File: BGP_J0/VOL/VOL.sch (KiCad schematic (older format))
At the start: 24 parts, among them P1 CONN_01X03, P2 CONN_01X02, P3 CONN_01X04, P4 CONN_01X03, Q1 J201, Q2 J201

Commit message: Schematics done, pcb layout pending
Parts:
- C2: value 10u -> 47u
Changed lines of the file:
@@
 	0    1    1    0
-$EndComp
-$Comp
-L CP1_Small C2
-U 1 1 5A6FC1F6
-P 3850 4600
-F 0 "C2" H 3860 4670 50  0000 L CNN
-F 1 "10u" H 3860 4520 50  0000 L CNN
-F 2 "Capacitors_Tantalum_SMD:TantalC_SizeR_EIA-2012" H 3850 4600 50  0001 C CNN
-F 3 "" H 3850 4600 50  0000 C CNN
-	1    3850 4600
-	1    0    0    -1
 $EndComp
 Wire Wire Line
@@
 	1    0    0    -1
 $EndComp
+$Comp
+L CP1_Small C2
+U 1 1 5A6FE715
+P 3850 4600
+F 0 "C2" H 3860 4670 50  0000 L CNN
+F 1 "47u" H 3860 4520 50  0000 L CNN
+F 2 "Capacitors_Tantalum_SMD:TantalC_SizeR_EIA-2012" H 3850 4600 50  0001 C CNN
+F 3 "" H 3850 4600 50  0000 C CNN
+	1    3850 4600
+	1    0    0    -1
+$EndComp

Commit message: PCB Layout done
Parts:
- removed P4: CONN_01X03, Connectors_JST:JST_PH_B3B-PH-K_03x2.00mm_Straight, symbol CONN_01X03
- added D1: D_Small, Diodes_SMD:SMA_Standard, symbol D_Small
- added P4: CONN_01X02, Connectors_JST:JST_PH_B2B-PH-K_02x2.00mm_Straight, symbol CONN_01X02
- Q1, Q2: value J201 -> J202; footprint TO_SOT_Packages_SMD:SOT-23 -> TO_SOT_Packages_SMD:SC-59
- R4: value 10k -> 12k
- R5: value 4.99k -> 6.8k
- R7: value 4.99k -> 10k
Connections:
- net Earth: now also C2.2, R3.2, D1.2 (A)
- net I_BY: now also P4.2 (P2)
- net O_BY: now also P4.1 (P1)
- net VCC: now also D1.1 (K)
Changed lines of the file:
@@
 P 4250 3350
 F 0 "Q1" H 4550 3400 50  0000 R CNN
-F 1 "J201" H 4600 3300 50  0000 R CNN
-F 2 "TO_SOT_Packages_SMD:SOT-23" H 4450 3450 50  0001 C CNN
+F 1 "J202" H 4600 3300 50  0000 R CNN
+F 2 "TO_SOT_Packages_SMD:SC-59" H 4450 3450 50  0001 C CNN
 F 3 "" H 4250 3350 50  0000 C CNN
 	1    4250 3350
@@
 P 4350 3000
 F 0 "R4" H 4380 3020 50  0000 L CNN
-F 1 "10k" H 4380 2960 50  0000 L CNN
+F 1 "12k" H 4380 2960 50  0000 L CNN
 F 2 "Resistors_SMD:R_0603_HandSoldering" H 4350 3000 50  0001 C CNN
 F 3 "" H 4350 3000 50  0000 C CNN
@@
 P 4350 3700
 F 0 "R5" H 4380 3720 50  0000 L CNN
-F 1 "4.99k" H 4380 3660 50  0000 L CNN
+F 1 "6.8k" H 4380 3660 50  0000 L CNN
 F 2 "Resistors_SMD:R_0603_HandSoldering" H 4350 3700 50  0001 C CNN
 F 3 "" H 4350 3700 50  0000 C CNN
@@
 P 5750 3150
 F 0 "Q2" H 6050 3200 50  0000 R CNN
-F 1 "J201" H 6100 3100 50  0000 R CNN
-F 2 "TO_SOT_Packages_SMD:SOT-23" H 5950 3250 50  0001 C CNN
+F 1 "J202" H 6100 3100 50  0000 R CNN
+F 2 "TO_SOT_Packages_SMD:SC-59" H 5950 3250 50  0001 C CNN
 F 3 "" H 5750 3150 50  0000 C CNN
 	1    5750 3150
@@
 P 5850 3550
 F 0 "R7" H 5880 3570 50  0000 L CNN
-F 1 "4.99k" H 5880 3510 50  0000 L CNN
+F 1 "10k" H 5880 3510 50  0000 L CNN
 F 2 "Resistors_SMD:R_0603_HandSoldering" H 5850 3550 50  0001 C CNN
 F 3 "" H 5850 3550 50  0000 C CNN
@@
 	3550 4700 3550 4750
 Wire Wire Line
-	3550 4750 3850 4750
+	3300 4750 3850 4750
 Wire Wire Line
 	3850 4750 3850 4700
@@
 $EndComp
 $Comp
-L CONN_01X03 P4
-U 1 1 5A6FC51C
-P 8400 4100
-F 0 "P4" H 8400 4300 50  0000 C CNN
-F 1 "CONN_01X03" V 8500 4100 50  0000 C CNN
-F 2 "Connectors_JST:JST_PH_B3B-PH-K_03x2.00mm_Straight" H 8400 4100 50  0001 C CNN
-F 3 "" H 8400 4100 50  0000 C CNN
-	1    8400 4100
-	1    0    0    -1
-$EndComp
-$Comp
-L Earth #PWR014
-U 1 1 5A6FC6BE
-P 8200 4200
-F 0 "#PWR014" H 8200 3950 50  0001 C CNN
-F 1 "Earth" H 8200 4050 50  0001 C CNN
-F 2 "" H 8200 4200 50  0000 C CNN
-F 3 "" H 8200 4200 50  0000 C CNN
-	1    8200 4200
-	1    0    0    -1
-$EndComp
-$Comp
 L CP1_Small C2
 U 1 1 5A6FE715
@@
 	1    0    0    -1
 $EndComp
+$Comp
+L CONN_01X02 P4
+U 1 1 5A712F0B
+P 8400 4050
+F 0 "P4" H 8400 4200 50  0000 C CNN
+F 1 "CONN_01X02" V 8500 4050 50  0000 C CNN
+F 2 "Connectors_JST:JST_PH_B2B-PH-K_02x2.00mm_Straight" H 8400 4050 50  0001 C CNN
+F 3 "" H 8400 4050 50  0000 C CNN
+	1    8400 4050
+	1    0    0    -1
+$EndComp
+$Comp
+L Earth #PWR014
+U 1 1 5A71310A
+P 3550 4750
+F 0 "#PWR014" H 3550 4500 50  0001 C CNN
+F 1 "Earth" H 3550 4600 50  0001 C CNN
+F 2 "" H 3550 4750 50  0000 C CNN
+F 3 "" H 3550 4750 50  0000 C CNN
+	1    3550 4750
+	1    0    0    -1
+$EndComp
+$Comp
+L D_Small D1
+U 1 1 5A71407F
+P 3300 4600
+F 0 "D1" H 3250 4680 50  0000 L CNN
+F 1 "D_Small" H 3150 4520 50  0000 L CNN
+F 2 "Diodes_SMD:SMA_Standard" V 3300 4600 50  0001 C CNN
+F 3 "" V 3300 4600 50  0000 C CNN
+	1    3300 4600
+	0    1    1    0
+$EndComp
+Wire Wire Line
+	3300 4500 3300 4150
+Wire Wire Line
+	3300 4150 3550 4150
+Wire Wire Line
+	3300 4700 3300 4750
+Connection ~ 3550 4750
 $EndSCHEMATC

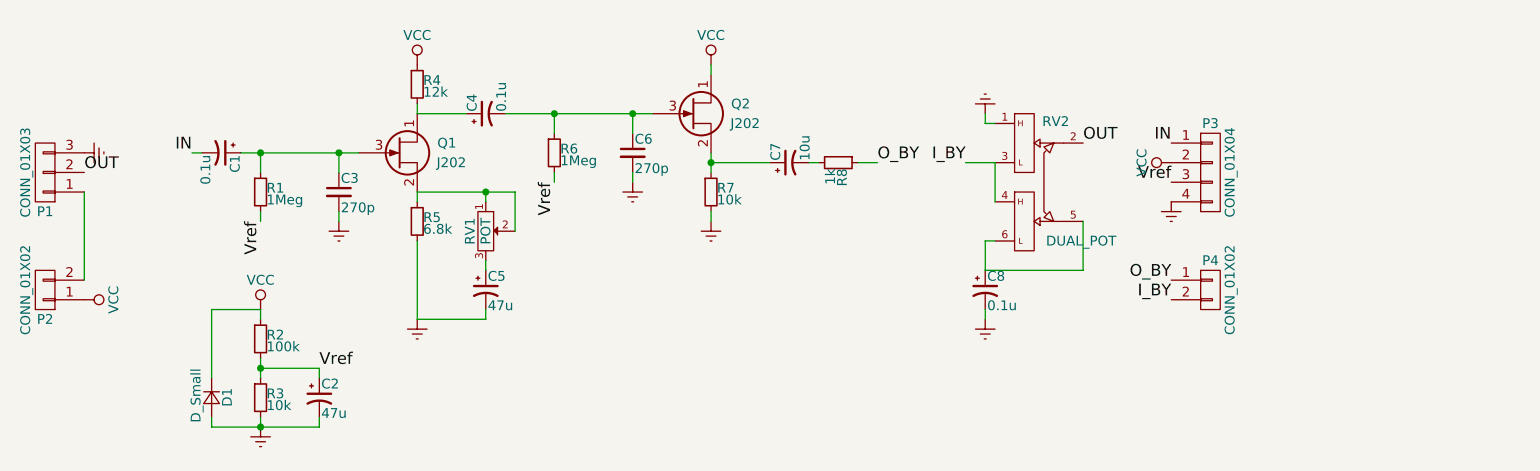
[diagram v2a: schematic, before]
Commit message: Changed POT, parallel VOL pot conn for offboard pot
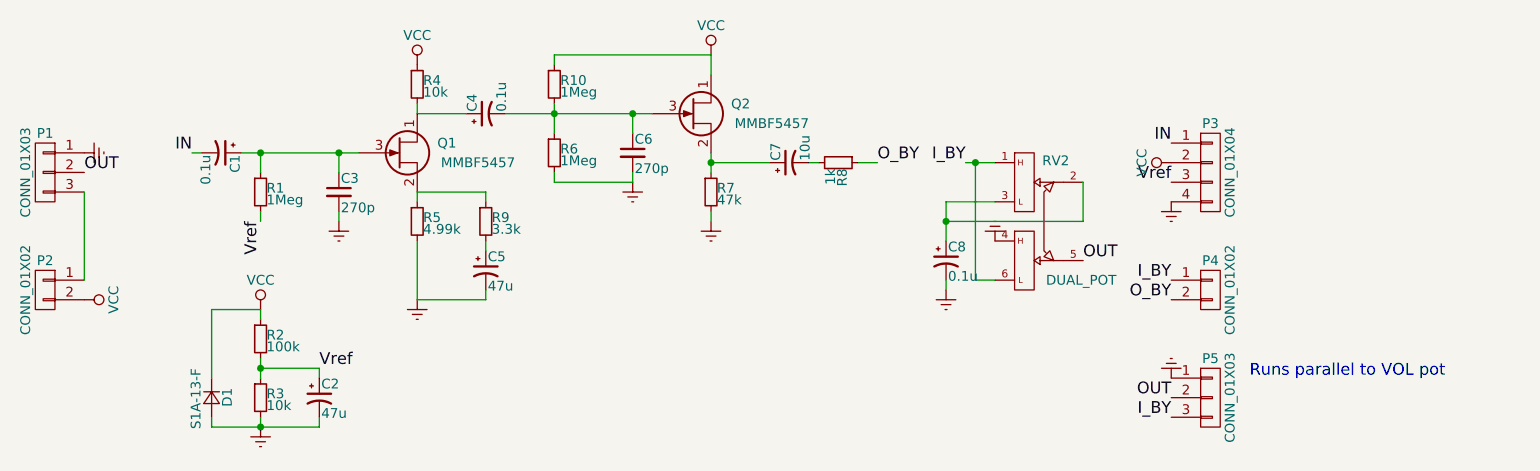
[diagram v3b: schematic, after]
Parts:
- removed RV1: POT, Potentiometers:Potentiometer_Trimmer_Bourns_3296W, symbol POT
- added P5: CONN_01X03, Connectors_JST:JST_PH_B3B-PH-K_03x2.00mm_Straight, symbol CONN_01X03
- added R10: 1Meg, Resistors_SMD:R_0603_HandSoldering, symbol R_Small
- added R9: 3.3k, Resistors_SMD:R_0603_HandSoldering, symbol R_Small
- D1: value D_Small -> S1A-13-F
- Q1, Q2: value J202 -> MMBF5457
- R4: value 12k -> 10k
- R5: value 6.8k -> 4.99k
- R7: value 10k -> 47k
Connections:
- net Earth: now also P1.1 (P1), R6.2, RV2.4, P5.1 (P1); no longer P1.3 (P3), RV2.1
- net I_BY: now also P4.1 (P1), RV2.1, RV2.6, P5.3 (P3); no longer P4.2 (P2), RV2.3, RV2.4
- net OUT: now also RV2.5, P5.2 (P2); no longer RV2.2
- net O_BY: now also P4.2 (P2); no longer P4.1 (P1)
- net VCC: now also P2.2 (P2), R10.1; no longer P2.1 (P1)
- net Vref: no longer R6.2
- net at Q1.2 (S), R5.1: now also R9.1
- net at C5.1: now also R9.2
- net at C4.2, C6.1, Q2.3 (G)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: now also R10.2
- new net: P1.3 (P3), P2.1 (P1)
- new net: C8.1, RV2.2, RV2.3
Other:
- note added: "Runs parallel to VOL pot"
- moved on the sheet: C5, C8, RV2
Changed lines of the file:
@@
 F 3 "" H 2450 3450 50  0000 C CNN
 	1    2450 3450
-	-1   0    0    1
+	-1   0    0    -1
 $EndComp
 $Comp
@@
 F 3 "" H 2450 4050 50  0000 C CNN
 	1    2450 4050
-	-1   0    0    1
+	-1   0    0    -1
 $EndComp
 Wire Wire Line
@@
 P 4250 3350
 F 0 "Q1" H 4550 3400 50  0000 R CNN
-F 1 "J202" H 4600 3300 50  0000 R CNN
+F 1 "MMBF5457" H 4850 3300 50  0000 R CNN
 F 2 "TO_SOT_Packages_SMD:SC-59" H 4450 3450 50  0001 C CNN
 F 3 "" H 4250 3350 50  0000 C CNN
@@
 P 4350 3000
 F 0 "R4" H 4380 3020 50  0000 L CNN
-F 1 "12k" H 4380 2960 50  0000 L CNN
+F 1 "10k" H 4380 2960 50  0000 L CNN
 F 2 "Resistors_SMD:R_0603_HandSoldering" H 4350 3000 50  0001 C CNN
 F 3 "" H 4350 3000 50  0000 C CNN
@@
 P 4350 3700
 F 0 "R5" H 4380 3720 50  0000 L CNN
-F 1 "6.8k" H 4380 3660 50  0000 L CNN
+F 1 "4.99k" H 4380 3660 50  0000 L CNN
 F 2 "Resistors_SMD:R_0603_HandSoldering" H 4350 3700 50  0001 C CNN
 F 3 "" H 4350 3700 50  0000 C CNN
@@
 $EndComp
 $Comp
-L POT RV1
-U 1 1 5A6FB689
-P 4700 3750
-F 0 "RV1" H 4700 3670 50  0000 C CNN
-F 1 "POT" H 4700 3750 50  0000 C CNN
-F 2 "Potentiometers:Potentiometer_Trimmer_Bourns_3296W" H 4700 3750 50  0001 C CNN
-F 3 "" H 4700 3750 50  0000 C CNN
-	1    4700 3750
-	0    1    1    0
-$EndComp
-$Comp
 L CP1_Small C5
 U 1 1 5A6FB719
-P 4700 4050
-F 0 "C5" H 4710 4120 50  0000 L CNN
-F 1 "47u" H 4710 3970 50  0000 L CNN
-F 2 "Capacitors_Tantalum_SMD:TantalC_SizeR_EIA-2012" H 4700 4050 50  0001 C CNN
-F 3 "" H 4700 4050 50  0000 C CNN
-	1    4700 4050
+P 4700 3950
+F 0 "C5" H 4710 4020 50  0000 L CNN
+F 1 "47u" H 4710 3870 50  0000 L CNN
+F 2 "Capacitors_Tantalum_SMD:TantalC_SizeR_EIA-2012" H 4700 3950 50  0001 C CNN
+F 3 "" H 4700 3950 50  0000 C CNN
+	1    4700 3950
 	1    0    0    -1
 $EndComp
@@
 L Earth #PWR04
 U 1 1 5A6FB793
-P 4350 4200
-F 0 "#PWR04" H 4350 3950 50  0001 C CNN
-F 1 "Earth" H 4350 4050 50  0001 C CNN
-F 2 "" H 4350 4200 50  0000 C CNN
-F 3 "" H 4350 4200 50  0000 C CNN
-	1    4350 4200
-	1    0    0    -1
-$EndComp
-Wire Wire Line
-	4350 4200 4700 4200
-Wire Wire Line
-	4700 4200 4700 4150
-Wire Wire Line
-	4350 4200 4350 3800
+P 4350 4100
+F 0 "#PWR04" H 4350 3850 50  0001 C CNN
+F 1 "Earth" H 4350 3950 50  0001 C CNN
+F 2 "" H 4350 4100 50  0000 C CNN
+F 3 "" H 4350 4100 50  0000 C CNN
+	1    4350 4100
+	1    0    0    -1
+$EndComp
+Wire Wire Line
+	4350 4100 4700 4100
+Wire Wire Line
+	4700 4100 4700 4050
 Wire Wire Line
 	4350 3550 4350 3600
 Wire Wire Line
-	4350 3550 4850 3550
-Wire Wire Line
-	4700 3550 4700 3600
-Wire Wire Line
-	4700 3900 4700 3950
+	4700 3800 4700 3850
 Wire Wire Line
 	4350 3100 4350 3150
@@
 	1    0    0    -1
 $EndComp
-Wire Wire Line
-	4850 3550 4850 3750
-Connection ~ 4700 3550
 $Comp
 L CP1_Small C4
@@
 P 5750 3150
 F 0 "Q2" H 6050 3200 50  0000 R CNN
-F 1 "J202" H 6100 3100 50  0000 R CNN
+F 1 "MMBF5457" H 6350 3100 50  0000 R CNN
 F 2 "TO_SOT_Packages_SMD:SC-59" H 5950 3250 50  0001 C CNN
 F 3 "" H 5750 3150 50  0000 C CNN
@@
 	1    0    0    -1
 $EndComp
-Text Label 5050 3500 3    60   ~ 0
-Vref
 Wire Wire Line
 	4800 3150 5550 3150
 Wire Wire Line
-	5050 3150 5050 3250
+	5050 3100 5050 3250
 Wire Wire Line
 	5450 3150 5450 3250
@@
 L VCC #PWR07
 U 1 1 5A6FBF1D
-P 5850 2900
-F 0 "#PWR07" H 5850 2750 50  0001 C CNN
-F 1 "VCC" H 5850 3050 50  0000 C CNN
-F 2 "" H 5850 2900 50  0000 C CNN
-F 3 "" H 5850 2900 50  0000 C CNN
-	1    5850 2900
-	1    0    0    -1
-$EndComp
-Wire Wire Line
-	5850 2900 5850 2950
+P 5850 2850
+F 0 "#PWR07" H 5850 2700 50  0001 C CNN
+F 1 "VCC" H 5850 3000 50  0000 C CNN
+F 2 "" H 5850 2850 50  0000 C CNN
+F 3 "" H 5850 2850 50  0000 C CNN
+	1    5850 2850
+	1    0    0    -1
+$EndComp
+Wire Wire Line
+	5850 2850 5850 2950
 $Comp
 L R_Small R7
@@
 P 5850 3550
 F 0 "R7" H 5880 3570 50  0000 L CNN
-F 1 "10k" H 5880 3510 50  0000 L CNN
+F 1 "47k" H 5880 3510 50  0000 L CNN
 F 2 "Resistors_SMD:R_0603_HandSoldering" H 5850 3550 50  0001 C CNN
 F 3 "" H 5850 3550 50  0000 C CNN
@@
 L DUAL_POT RV2
 U 1 1 5A6FCAF4
-P 7450 3500
-F 0 "RV2" H 7610 3810 50  0000 C CNN
-F 1 "DUAL_POT" H 7740 3200 50  0000 C CNN
-F 2 "LIBS:Potentiometer_Alpha_Double_Vertical_Dual_Shaft" H 7450 3500 50  0001 C CNN
-F 3 "" H 7450 3500 50  0000 C CNN
-	1    7450 3500
-	1    0    0    -1
-$EndComp
-Wire Wire Line
-	7300 3400 7150 3400
-Wire Wire Line
-	7300 3200 7250 3200
-Wire Wire Line
-	7250 3200 7250 3150
+P 7450 3700
+F 0 "RV2" H 7610 4010 50  0000 C CNN
+F 1 "DUAL_POT" H 7740 3400 50  0000 C CNN
+F 2 "LIBS:Potentiometer_Alpha_Double_Vertical_Dual_Shaft" H 7450 3700 50  0001 C CNN
+F 3 "" H 7450 3700 50  0000 C CNN
+	1    7450 3700
+	1    0    0    -1
+$EndComp
 $Comp
 L Earth #PWR010
-U 1 1 5A6FCC4F
-P 7250 3150
-F 0 "#PWR010" H 7250 2900 50  0001 C CNN
-F 1 "Earth" H 7250 3000 50  0001 C CNN
-F 2 "" H 7250 3150 50  0000 C CNN
-F 3 "" H 7250 3150 50  0000 C CNN
-	1    7250 3150
-	-1   0    0    1
-$EndComp
-$Comp
-L Earth #PWR011
 U 1 1 5A6FCD99
-P 7250 4200
-F 0 "#PWR011" H 7250 3950 50  0001 C CNN
-F 1 "Earth" H 7250 4050 50  0001 C CNN
-F 2 "" H 7250 4200 50  0000 C CNN
-F 3 "" H 7250 4200 50  0000 C CNN
-	1    7250 4200
-	1    0    0    -1
-$EndComp
-Wire Wire Line
-	7250 4150 7250 4200
-Wire Wire Line
-	7250 3800 7250 3950
-Wire Wire Line
-	7250 3800 7300 3800
-Wire Wire Line
-	7250 3950 7750 3950
-Wire Wire Line
-	7750 3950 7750 3700
-Wire Wire Line
-	7300 3600 7300 3400
+P 7050 4050
+F 0 "#PWR010" H 7050 3800 50  0001 C CNN
+F 1 "Earth" H 7050 3900 50  0001 C CNN
+F 2 "" H 7050 4050 50  0000 C CNN
+F 3 "" H 7050 4050 50  0000 C CNN
+	1    7050 4050
+	1    0    0    -1
+$EndComp
+Wire Wire Line
+	7050 4000 7050 4050
 $Comp
 L CP1_Small C7
@@
 Wire Wire Line
 	6400 3400 6350 3400
-Text Label 7750 3300 0    60   ~ 0
+Text Label 7750 3900 0    60   ~ 0
 OUT
 Text Label 8200 3300 2    60   ~ 0
@@
 $EndComp
 $Comp
-L VCC #PWR012
+L VCC #PWR011
 U 1 1 5A6FD5A8
 P 8200 3400
-F 0 "#PWR012" H 8200 3250 50  0001 C CNN
+F 0 "#PWR011" H 8200 3250 50  0001 C CNN
 F 1 "VCC" H 8200 3550 50  0000 C CNN
 F 2 "" H 8200 3400 50  0000 C CNN
@@
 Vref
 $Comp
-L Earth #PWR013
+L Earth #PWR012
 U 1 1 5A6FD63F
 P 8200 3600
-F 0 "#PWR013" H 8200 3350 50  0001 C CNN
+F 0 "#PWR012" H 8200 3350 50  0001 C CNN
 F 1 "Earth" H 8200 3450 50  0001 C CNN
 F 2 "" H 8200 3600 50  0000 C CNN
@@
 	1    0    0    -1
 $EndComp
+Text Label 8200 4100 2    60   ~ 0
+O_BY
 Text Label 8200 4000 2    60   ~ 0
-O_BY
-Text Label 8200 4100 2    60   ~ 0
 I_BY
 $Comp
 L CP1_Small C8
 U 1 1 5A6FE796
-P 7250 4050
-F 0 "C8" H 7260 4120 50  0000 L CNN
-F 1 "0.1u" H 7260 3970 50  0000 L CNN
-F 2 "Capacitors_Tantalum_SMD:TantalC_SizeR_EIA-2012" H 7250 4050 50  0001 C CNN
-F 3 "" H 7250 4050 50  0000 C CNN
-	1    7250 4050
+P 7050 3900
+F 0 "C8" H 7060 3970 50  0000 L CNN
+F 1 "0.1u" H 7060 3820 50  0000 L CNN
+F 2 "Capacitors_Tantalum_SMD:TantalC_SizeR_EIA-2012" H 7050 3900 50  0001 C CNN
+F 3 "" H 7050 3900 50  0000 C CNN
+	1    7050 3900
 	1    0    0    -1
 $EndComp
@@
 $EndComp
 $Comp
-L Earth #PWR014
+L Earth #PWR013
 U 1 1 5A71310A
 P 3550 4750
-F 0 "#PWR014" H 3550 4500 50  0001 C CNN
+F 0 "#PWR013" H 3550 4500 50  0001 C CNN
 F 1 "Earth" H 3550 4600 50  0001 C CNN
 F 2 "" H 3550 4750 50  0000 C CNN
@@
 P 3300 4600
 F 0 "D1" H 3250 4680 50  0000 L CNN
-F 1 "D_Small" H 3150 4520 50  0000 L CNN
+F 1 "S1A-13-F" H 3150 4520 50  0000 L CNN
 F 2 "Diodes_SMD:SMA_Standard" V 3300 4600 50  0001 C CNN
 F 3 "" V 3300 4600 50  0000 C CNN
@@
 	3300 4700 3300 4750
 Connection ~ 3550 4750
+$Comp
+L R_Small R9
+U 1 1 5A7248C9
+P 4700 3700
+F 0 "R9" H 4730 3720 50  0000 L CNN
+F 1 "3.3k" H 4730 3660 50  0000 L CNN
+F 2 "Resistors_SMD:R_0603_HandSoldering" H 4700 3700 50  0001 C CNN
+F 3 "" H 4700 3700 50  0000 C CNN
+	1    4700 3700
+	1    0    0    -1
+$EndComp
+Wire Wire Line
+	4350 4100 4350 3800
+Wire Wire Line
+	4350 3550 4700 3550
+Wire Wire Line
+	4700 3550 4700 3600
+$Comp
+L R_Small R10
+U 1 1 5A724BC7
+P 5050 3000
+F 0 "R10" H 5080 3020 50  0000 L CNN
+F 1 "1Meg" H 5080 2960 50  0000 L CNN
+F 2 "Resistors_SMD:R_0603_HandSoldering" H 5050 3000 50  0001 C CNN
+F 3 "" H 5050 3000 50  0000 C CNN
+	1    5050 3000
+	1    0    0    -1
+$EndComp
+Wire Wire Line
+	5850 2850 5050 2850
+Wire Wire Line
+	5050 2850 5050 2900
+Wire Wire Line
+	5450 3500 5050 3500
+$Comp
+L CONN_01X03 P5
+U 1 1 5A725119
+P 8400 4600
+F 0 "P5" H 8400 4800 50  0000 C CNN
+F 1 "CONN_01X03" V 8500 4600 50  0000 C CNN
+F 2 "Connectors_JST:JST_PH_B3B-PH-K_03x2.00mm_Straight" H 8400 4600 50  0001 C CNN
+F 3 "" H 8400 4600 50  0000 C CNN
+	1    8400 4600
+	1    0    0    -1
+$EndComp
+$Comp
+L Earth #PWR014
+U 1 1 5A7251E9
+P 8200 4500
+F 0 "#PWR014" H 8200 4250 50  0001 C CNN
+F 1 "Earth" H 8200 4350 50  0001 C CNN
+F 2 "" H 8200 4500 50  0000 C CNN
+F 3 "" H 8200 4500 50  0000 C CNN
+	1    8200 4500
+	-1   0    0    1
+$EndComp
+Text Label 8200 4700 2    60   ~ 0
+I_BY
+Text Label 8200 4600 2    60   ~ 0
+OUT
+$Comp
+L Earth #PWR015
+U 1 1 5A72580A
+P 7300 3800
+F 0 "#PWR015" H 7300 3550 50  0001 C CNN
+F 1 "Earth" H 7300 3650 50  0001 C CNN
+F 2 "" H 7300 3800 50  0000 C CNN
+F 3 "" H 7300 3800 50  0000 C CNN
+	1    7300 3800
+	-1   0    0    1
+$EndComp
+Wire Wire Line
+	7050 3600 7300 3600
+Wire Wire Line
+	7300 3400 7150 3400
+Wire Wire Line
+	7200 3400 7200 4000
+Wire Wire Line
+	7200 4000 7300 4000
+Connection ~ 7200 3400
+Text Notes 8600 4500 0    60   ~ 0
+Runs parallel to VOL pot
+Wire Wire Line
+	7050 3700 7750 3700
+Wire Wire Line
+	7750 3700 7750 3500
+Wire Wire Line
+	7050 3800 7050 3600
+Connection ~ 7050 3700
 $EndSCHEMATC

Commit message: Some cleanup, and gain stage changes
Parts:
- R4: value 10k -> 12k
- R5: value 4.99k -> 6.8k
- R9: value 3.3k -> 2.7k
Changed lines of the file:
@@
 P 4350 3000
 F 0 "R4" H 4380 3020 50  0000 L CNN
-F 1 "10k" H 4380 2960 50  0000 L CNN
+F 1 "12k" H 4380 2960 50  0000 L CNN
 F 2 "Resistors_SMD:R_0603_HandSoldering" H 4350 3000 50  0001 C CNN
 F 3 "" H 4350 3000 50  0000 C CNN
@@
 P 4350 3700
 F 0 "R5" H 4380 3720 50  0000 L CNN
-F 1 "4.99k" H 4380 3660 50  0000 L CNN
+F 1 "6.8k" H 4380 3660 50  0000 L CNN
 F 2 "Resistors_SMD:R_0603_HandSoldering" H 4350 3700 50  0001 C CNN
 F 3 "" H 4350 3700 50  0000 C CNN
@@
 P 4700 3700
 F 0 "R9" H 4730 3720 50  0000 L CNN
-F 1 "3.3k" H 4730 3660 50  0000 L CNN
+F 1 "2.7k" H 4730 3660 50  0000 L CNN
 F 2 "Resistors_SMD:R_0603_HandSoldering" H 4700 3700 50  0001 C CNN
 F 3 "" H 4700 3700 50  0000 C CNN

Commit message: Slight buffer change
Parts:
- R10: value 1Meg -> 1.5Meg
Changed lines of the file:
@@
 P 5050 3000
 F 0 "R10" H 5080 3020 50  0000 L CNN
-F 1 "1Meg" H 5080 2960 50  0000 L CNN
+F 1 "1.5Meg" H 5080 2960 50  0000 L CNN
 F 2 "Resistors_SMD:R_0603_HandSoldering" H 5050 3000 50  0001 C CNN
 F 3 "" H 5050 3000 50  0000 C CNN

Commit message: Pots were out by a little, changed PCBs accordingly
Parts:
- R7: value 47k -> 24.9k
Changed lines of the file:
@@
 P 5850 3550
 F 0 "R7" H 5880 3570 50  0000 L CNN
-F 1 "47k" H 5880 3510 50  0000 L CNN
+F 1 "24.9k" H 5880 3510 50  0000 L CNN
 F 2 "Resistors_SMD:R_0603_HandSoldering" H 5850 3550 50  0001 C CNN
 F 3 "" H 5850 3550 50  0000 C CNN

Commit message: Changed Gain structure a bit
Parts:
- R4: value 12k -> 10k
- R5: value 6.8k -> 4.99k
- R8: value 1k -> 100
- R9: value 2.7k -> 4.99k
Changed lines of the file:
@@
 P 4350 3000
 F 0 "R4" H 4380 3020 50  0000 L CNN
-F 1 "12k" H 4380 2960 50  0000 L CNN
+F 1 "10k" H 4380 2960 50  0000 L CNN
 F 2 "Resistors_SMD:R_0603_HandSoldering" H 4350 3000 50  0001 C CNN
 F 3 "" H 4350 3000 50  0000 C CNN
@@
 P 4350 3700
 F 0 "R5" H 4380 3720 50  0000 L CNN
-F 1 "6.8k" H 4380 3660 50  0000 L CNN
+F 1 "4.99k" H 4380 3660 50  0000 L CNN
 F 2 "Resistors_SMD:R_0603_HandSoldering" H 4350 3700 50  0001 C CNN
 F 3 "" H 4350 3700 50  0000 C CNN
@@
 P 6500 3400
 F 0 "R8" H 6530 3420 50  0000 L CNN
-F 1 "1k" H 6530 3360 50  0000 L CNN
+F 1 "100" H 6530 3360 50  0000 L CNN
 F 2 "Resistors_SMD:R_0603_HandSoldering" H 6500 3400 50  0001 C CNN
 F 3 "" H 6500 3400 50  0000 C CNN
@@
 P 4700 3700
 F 0 "R9" H 4730 3720 50  0000 L CNN
-F 1 "2.7k" H 4730 3660 50  0000 L CNN
+F 1 "4.99k" H 4730 3660 50  0000 L CNN
 F 2 "Resistors_SMD:R_0603_HandSoldering" H 4700 3700 50  0001 C CNN
 F 3 "" H 4700 3700 50  0000 C CNN

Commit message: Value and gain structure tweak
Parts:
- R9: value 4.99k -> 1.8k
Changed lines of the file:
@@
 P 4700 3700
 F 0 "R9" H 4730 3720 50  0000 L CNN
-F 1 "4.99k" H 4730 3660 50  0000 L CNN
+F 1 "1.8k" H 4730 3660 50  0000 L CNN
 F 2 "Resistors_SMD:R_0603_HandSoldering" H 4700 3700 50  0001 C CNN
 F 3 "" H 4700 3700 50  0000 C CNN
